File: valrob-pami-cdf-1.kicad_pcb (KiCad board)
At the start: 4 copper layers, 58 x 50 mm, 139 parts, among them J1 Conn_01x04, J2 USB_C_Receptacle_USB2.0_14P, J3 Conn_01x02, J4 Conn_01x04_Pin, J5 Conn_01x06, M1 Motor_Servo, M2 Stepper_Motor_bipolar, M3 Stepper_Motor_bipolar, Q1 Q_NMOS, Q2 Q_NMOS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

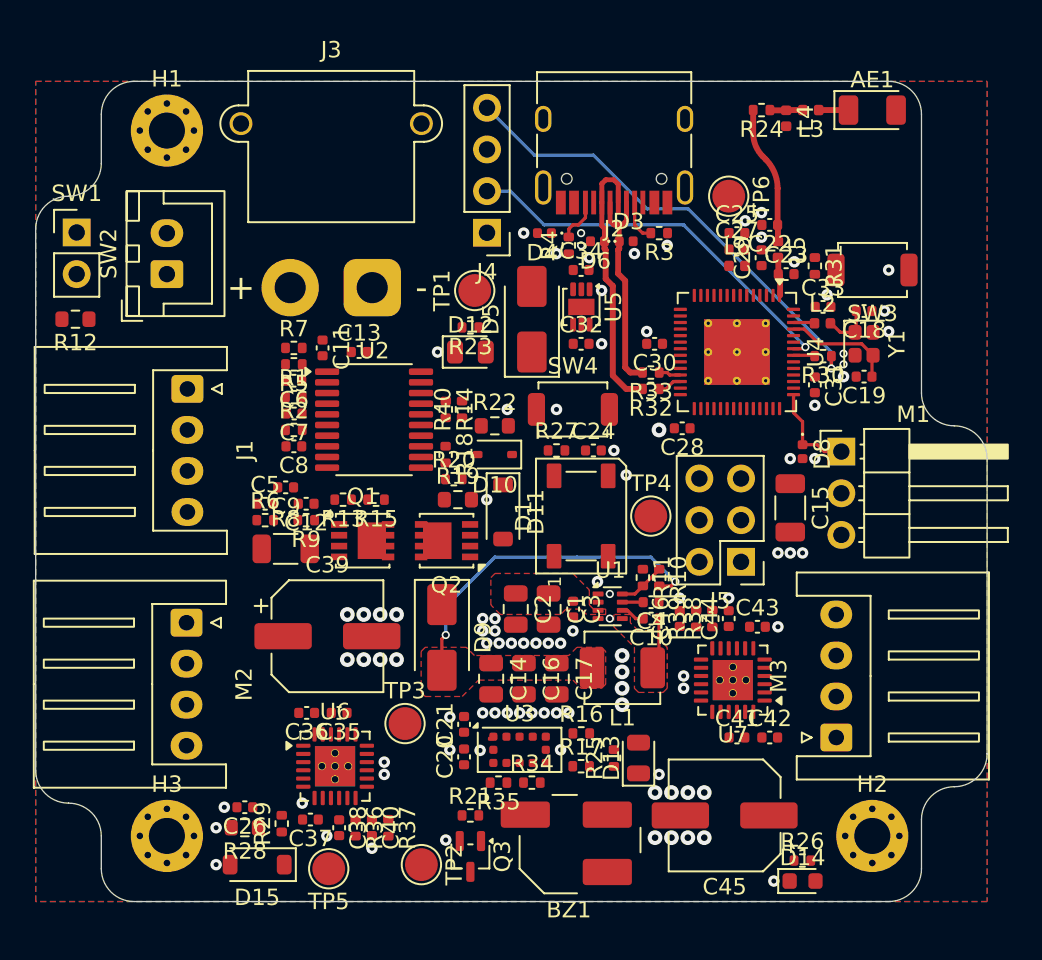
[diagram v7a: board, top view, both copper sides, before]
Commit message: pcb: add bms routing
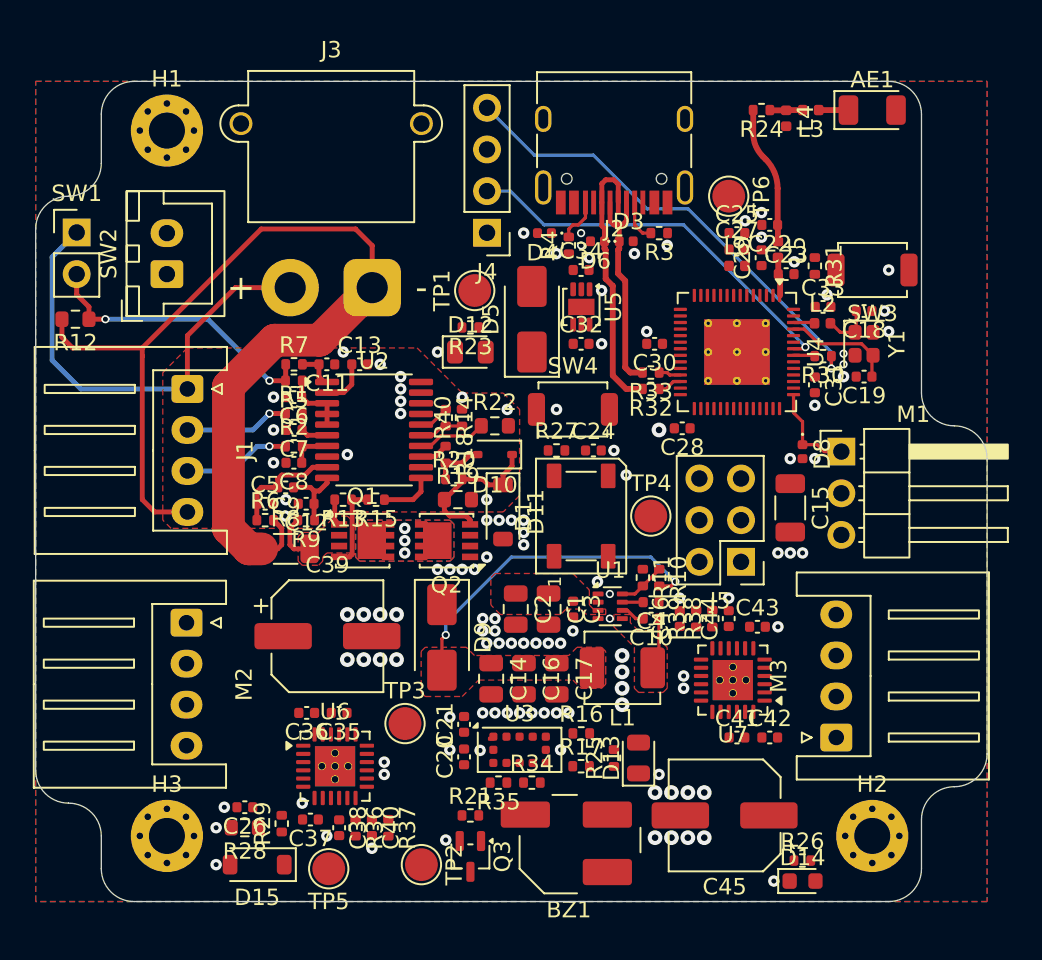
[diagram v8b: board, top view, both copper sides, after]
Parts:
- moved C11 1.03 mm to (143.8, 90.2), turned to 180 degrees
- moved R7 1.00 mm to (141.8, 90.2)
- moved C6 1.00 mm to (141.7, 92.2)
- moved C7 1.00 mm to (141.8, 94.2)
- moved C8 1.00 mm to (141.7, 96.2)
- moved R1 1.00 mm to (141.7, 93.2)
- moved R2 1.00 mm to (141.7, 95.2)
- moved R5 1.00 mm to (141.7, 91.2)
- moved C13 0.75 mm to (145.8, 90.2)
- moved U2 0.62 mm to (146.6, 94.2)
- moved R14 0.50 mm to (151.0, 93.5)
- moved R40 0.50 mm to (152.0, 93.5)
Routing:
- net BGND: track 0.00 -> 64.1 mm, vias 0 -> 13
- net +BATT: track 0.00 -> 28.1 mm
- net Net-(SW1-B): track 0.00 -> 17.6 mm, vias 0 -> 2
- net Net-(D10-K): track 0.00 -> 9.16 mm
- net Net-(U2-SRP): track 0.00 -> 6.93 mm
- net Net-(J1-Pin_3): track 0.00 -> 6.60 mm, vias 0 -> 1
- net Net-(J1-Pin_2): track 0.00 -> 6.39 mm, vias 0 -> 1
- net Net-(Q1-G): track 0.00 -> 5.20 mm
- net Net-(Q1-S-Pad1): track 0.00 -> 4.63 mm
- net Net-(U2-SRN): track 0.00 -> 4.44 mm
- net Net-(U2-LD): track 0.00 -> 4.18 mm
- net Net-(U2-VC3): track 0.00 -> 4.01 mm
- net Net-(U2-DSG): track 0.00 -> 3.27 mm
- net Net-(D10-A): track 0.00 -> 3.16 mm
- net Net-(U2-AVDD): track 0.00 -> 2.94 mm
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- added copper zone on F.Cu, net BGND
- added copper zone on In1.Cu, net BGND
- added copper zone on B.Cu, net Net-(Q1-D)
- added copper zone on F.Cu, net Net-(Q1-D)
- added copper zone on F.Cu, net Net-(Q1-S-Pad1)
